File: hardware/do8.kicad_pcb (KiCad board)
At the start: 4 copper layers, 100 x 85 mm, 116 parts, among them J101 TNG-Power-TOP, J102 TNG-Power-BTM, J103 TNG-Data-TOP, J104 TNG-Data-BTM, P102 Debug, P103 PE, P201 OUTPUT0, P202 OUTPUT1, P203 OUTPUT2, P204 OUTPUT3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

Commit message: completely routed
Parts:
- moved Fiducial_Mark 2.00 mm to (101.8, 145.5) (x2)
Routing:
- net VCC: track 31.1 -> 167.2 mm, vias 8 -> 53
- net AGND: track 59.6 -> 163.3 mm, vias 12 -> 95
- net Net-(C202-Pad2): track 34.7 -> 75.1 mm
- net Net-(C211-Pad2): track 36.2 -> 74.1 mm
- net Net-(C203-Pad2): track 25.1 -> 56.6 mm
- net Net-(C209-Pad2): track 25.2 -> 56.1 mm
- net Net-(C121-Pad1): track 19.6 -> 49.9 mm
- net Net-(C120-Pad2): track 13.8 -> 42.1 mm
- net Net-(C204-Pad2): track 21.0 -> 48.1 mm
- net Net-(C119-Pad2): track 11.5 -> 38.1 mm
- net Net-(C207-Pad2): track 20.2 -> 46.3 mm
- net VO: track 33.6 -> 59.0 mm
- net Net-(C206-Pad2): track 12.9 -> 31.9 mm
- net Net-(C205-Pad2): track 12.8 -> 31.4 mm
- net VCCPWRA: track 57.1 -> 62.8 mm
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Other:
- board text removed: "Fläche zur Kühlung mit VCC durchnageln"

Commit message: outline update
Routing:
- net ~CLK: track 57.6 -> 57.0 mm
- net SDO: track 56.0 -> 55.4 mm
- net LED6: track 66.2 -> 65.6 mm
- net ~SS: track 58.8 -> 58.2 mm
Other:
- outline, holes or cut-outs redrawn
- board text added: "DI0"
- board text added: "DI1"
- board text added: "DI2"
- board text added: "DI3"
- board text added: "DI4"
- board text added: "DI5"
- board text added: "DI6"
- board text added: "DI7"
- board text added: "tinkerforge.com"
- board text removed: "DI 0"
- board text removed: "DI 1"
- board text removed: "DI 2"
- board text removed: "DI 3"
- board text removed: "DI 4"
- board text removed: "DI 5"
- board text removed: "DI 6"
- board text removed: "DI 7"

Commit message: fix name
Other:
- board text added: "DO 8P REV 1.0"
- board text removed: "DO8 1.0"
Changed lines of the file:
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@@
     (effects (font (size 1 1) (thickness 0.15)) (justify mirror))
   )
-  (gr_text "DO8 1.0" (at 180.8 144.5) (layer F.SilkS)
+  (gr_text "DO 8P\nREV 1.0" (at 180.8 144.5) (layer F.SilkS)
     (effects (font (size 1 1) (thickness 0.15)))
   )

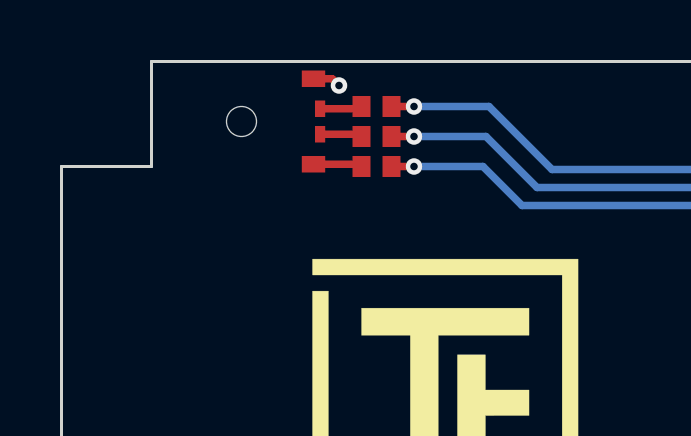
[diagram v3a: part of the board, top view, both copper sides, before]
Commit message: update rgb led drill diameter
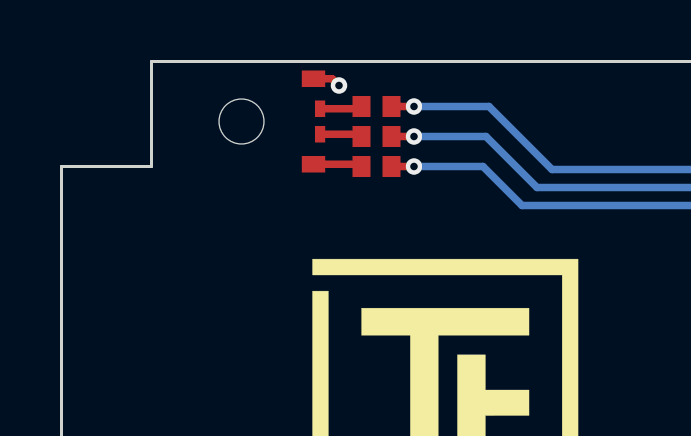
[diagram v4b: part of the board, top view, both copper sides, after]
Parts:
- LED101: footprint LED-RGB-LP -> kicad-libraries:LED-RGB-LP
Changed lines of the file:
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@@
     (add_net USB-DPC)
+  )
+  (module kicad-libraries:LED-RGB-LP (layer F.Cu)
+    (at 98.2 64.5 90)
+    (fp_text reference LED101 (at 0 0 90) (layer F.Fab)
+      (effects (font (size 0.15 0.15) (thickness 0.0375)))
+    )
+    (fp_text value EASV3015RGBA0 (at 0 -0.3 90) (layer F.Fab)
+      (effects (font (size 0.15 0.15) (thickness 0.0375)))
+    )
+    (fp_line (start -1 -1.4) (end 1 -1.4) (layer F.Fab) (width 0.1))
+    (fp_line (start 1 -1.4) (end 1 -8.4) (layer F.Fab) (width 0.1))
+    (fp_line (start 1 -8.4) (end -1 -8.4) (layer F.Fab) (width 0.1))
+    (fp_line (start -1 -8.4) (end -1 -1.4) (layer F.Fab) (width 0.1))
+    (fp_line (start -1.5 -0.5) (end -1.5 0.2) (layer F.Fab) (width 0.025))
+    (fp_line (start 1.5 -0.5) (end -1.5 -0.5) (layer F.Fab) (width 0.025))
+    (fp_line (start 1.5 0.2) (end 1.5 -0.5) (layer F.Fab) (width 0.025))
+    (fp_line (start -1.5 0.2) (end 1.5 0.2) (layer F.Fab) (width 0.025))
+    (fp_arc (start 0 -0.5) (end -0.8 -0.5) (angle 90) (layer F.Fab) (width 0.025))
+    (fp_arc (start 0 -0.5) (end 0 -1.3) (angle 90) (layer F.Fab) (width 0.025))
+    (pad 3 smd rect (at -0.425 0.22 90) (size 0.55 0.34) (layers F.Cu F.Paste F.Mask)
+      (net 33 "Net-(LED101-Pad3)"))
+    (pad 2 smd rect (at 0.425 0.22 90) (size 0.55 0.34) (layers F.Cu F.Paste F.Mask)
+      (net 32 "Net-(LED101-Pad2)"))
+    (pad 4 smd rect (at -1.425 0 90) (size 0.55 0.78) (layers F.Cu F.Paste F.Mask)
+      (net 31 "Net-(LED101-Pad4)"))
+    (pad 1 smd rect (at 1.425 0 90) (size 0.55 0.78) (layers F.Cu F.Paste F.Mask)
+      (net 2 3V3))
+    (pad "" np_thru_hole circle (at 0 -2.4 90) (size 1.5 1.5) (drill 1.5) (layers *.Cu *.Mask))
   )
   (module LED-LP (layer B.Cu)
@@
     )
   )
-  (module LED-RGB-LP (layer F.Cu)
-    (at 98.2 64.5 90)
-    (fp_text reference LED101 (at 0 0 90) (layer F.Fab)
-      (effects (font (size 0.15 0.15) (thickness 0.0375)))
-    )
-    (fp_text value EASV3015RGBA0 (at 0 -0.3 90) (layer F.Fab)
-      (effects (font (size 0.15 0.15) (thickness 0.0375)))
-    )
-    (fp_arc (start 0 -0.5) (end 0 -1.3) (angle 90) (layer F.Fab) (width 0.025))
-    (fp_arc (start 0 -0.5) (end -0.8 -0.5) (angle 90) (layer F.Fab) (width 0.025))
-    (fp_line (start -1.5 0.2) (end 1.5 0.2) (layer F.Fab) (width 0.025))
-    (fp_line (start 1.5 0.2) (end 1.5 -0.5) (layer F.Fab) (width 0.025))
-    (fp_line (start 1.5 -0.5) (end -1.5 -0.5) (layer F.Fab) (width 0.025))
-    (fp_line (start -1.5 -0.5) (end -1.5 0.2) (layer F.Fab) (width 0.025))
-    (fp_line (start -1 -8.4) (end -1 -1.4) (layer F.Fab) (width 0.1))
-    (fp_line (start 1 -8.4) (end -1 -8.4) (layer F.Fab) (width 0.1))
-    (fp_line (start 1 -1.4) (end 1 -8.4) (layer F.Fab) (width 0.1))
-    (fp_line (start -1 -1.4) (end 1 -1.4) (layer F.Fab) (width 0.1))
-    (pad "" np_thru_hole circle (at 0 -2.4 90) (size 1 1) (drill 1) (layers *.Cu *.Mask))
-    (pad 1 smd rect (at 1.425 0 90) (size 0.55 0.78) (layers F.Cu F.Paste F.Mask)
-      (net 2 3V3))
-    (pad 4 smd rect (at -1.425 0 90) (size 0.55 0.78) (layers F.Cu F.Paste F.Mask)
-      (net 31 "Net-(LED101-Pad4)"))
-    (pad 2 smd rect (at 0.425 0.22 90) (size 0.55 0.34) (layers F.Cu F.Paste F.Mask)
-      (net 32 "Net-(LED101-Pad2)"))
-    (pad 3 smd rect (at -0.425 0.22 90) (size 0.55 0.34) (layers F.Cu F.Paste F.Mask)
-      (net 33 "Net-(LED101-Pad3)"))
-  )
   (module kicad-libraries:Logo_TF_10x12 (layer F.Cu)

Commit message: fix inductor footprint
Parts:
- LED101: footprint kicad-libraries:LED-RGB-LP -> LED-RGB-LP
- turned T101 to 180 degrees
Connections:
- T101 pad 1: Net-(C120-Pad2) -> Net-(C121-Pad1)
- T101 pad 3: Net-(C121-Pad1) -> Net-(C120-Pad2)
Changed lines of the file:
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@@
     (add_net USB-DPC)
   )
-  (module kicad-libraries:LED-RGB-LP (layer F.Cu)
-    (at 98.2 64.5 90)
-    (fp_text reference LED101 (at 0 0 90) (layer F.Fab)
+  (module kicad-libraries:WE-SL5 (layer F.Cu)
+    (at 150.5 135.65 180)
+    (fp_text reference T101 (at 0 0.5) (layer F.Fab)
       (effects (font (size 0.15 0.15) (thickness 0.0375)))
     )
-    (fp_text value EASV3015RGBA0 (at 0 -0.3 90) (layer F.Fab)
+    (fp_text value 744273222 (at 0 -0.5) (layer F.Fab)
       (effects (font (size 0.15 0.15) (thickness 0.0375)))
     )
-    (fp_line (start -1 -1.4) (end 1 -1.4) (layer F.Fab) (width 0.1))
-    (fp_line (start 1 -1.4) (end 1 -8.4) (layer F.Fab) (width 0.1))
-    (fp_line (start 1 -8.4) (end -1 -8.4) (layer F.Fab) (width 0.1))
-    (fp_line (start -1 -8.4) (end -1 -1.4) (layer F.Fab) (width 0.1))
-    (fp_line (start -1.5 -0.5) (end -1.5 0.2) (layer F.Fab) (width 0.025))
-    (fp_line (start 1.5 -0.5) (end -1.5 -0.5) (layer F.Fab) (width 0.025))
-    (fp_line (start 1.5 0.2) (end 1.5 -0.5) (layer F.Fab) (width 0.025))
-    (fp_line (start -1.5 0.2) (end 1.5 0.2) (layer F.Fab) (width 0.025))
-    (fp_arc (start 0 -0.5) (end -0.8 -0.5) (angle 90) (layer F.Fab) (width 0.025))
-    (fp_arc (start 0 -0.5) (end 0 -1.3) (angle 90) (layer F.Fab) (width 0.025))
-    (pad 3 smd rect (at -0.425 0.22 90) (size 0.55 0.34) (layers F.Cu F.Paste F.Mask)
-      (net 33 "Net-(LED101-Pad3)"))
-    (pad 2 smd rect (at 0.425 0.22 90) (size 0.55 0.34) (layers F.Cu F.Paste F.Mask)
-      (net 32 "Net-(LED101-Pad2)"))
-    (pad 4 smd rect (at -1.425 0 90) (size 0.55 0.78) (layers F.Cu F.Paste F.Mask)
-      (net 31 "Net-(LED101-Pad4)"))
-    (pad 1 smd rect (at 1.425 0 90) (size 0.55 0.78) (layers F.Cu F.Paste F.Mask)
-      (net 2 3V3))
-    (pad "" np_thru_hole circle (at 0 -2.4 90) (size 1.5 1.5) (drill 1.5) (layers *.Cu *.Mask))
+    (fp_line (start -5 4.4) (end -5 -4.4) (layer F.Fab) (width 0.1))
+    (fp_line (start 5 4.4) (end -5 4.4) (layer F.Fab) (width 0.1))
+    (fp_line (start 5 -4.4) (end 5 4.4) (layer F.Fab) (width 0.1))
+    (fp_line (start -5 -4.4) (end 5 -4.4) (layer F.Fab) (width 0.1))
+    (fp_circle (center -3.5 -2) (end -3.2 -1.7) (layer F.Fab) (width 0.1))
+    (pad 2 smd rect (at -3.81 3.11 180) (size 2.7 2.7) (layers F.Cu F.Paste F.Mask)
+      (net 53 AGNDA))
+    (pad 3 smd rect (at 3.81 3.11 180) (size 2.7 2.7) (layers F.Cu F.Paste F.Mask)
+      (net 64 "Net-(C120-Pad2)"))
+    (pad 4 smd rect (at 3.81 -3.11 180) (size 2.7 2.7) (layers F.Cu F.Paste F.Mask)
+      (net 45 "Net-(C119-Pad2)"))
+    (pad 1 smd rect (at -3.81 -3.11 180) (size 2.7 2.7) (layers F.Cu F.Paste F.Mask)
+      (net 56 "Net-(C121-Pad1)"))
+    (model ${KICAD_SYMBOL_DIR}/3d/Inductors/WE-SL5.wrl
+      (at (xyz 0 0 0))
+      (scale (xyz 1 1 1))
+      (rotate (xyz 0 0 0))
+    )
   )
   (module LED-LP (layer B.Cu)
@@
     )
   )
-  (module kicad-libraries:WE-SL5 (layer F.Cu)
-    (at 150.5 135.65)
-    (fp_text reference T101 (at 0 0.5) (layer F.Fab)
-      (effects (font (size 0.15 0.15) (thickness 0.0375)))
-    )
-    (fp_text value 744273222 (at 0 -0.5) (layer F.Fab)
-      (effects (font (size 0.15 0.15) (thickness 0.0375)))
-    )
-    (fp_line (start -5 4.4) (end -5 -4.4) (layer F.Fab) (width 0.1))
-    (fp_line (start 5 4.4) (end -5 4.4) (layer F.Fab) (width 0.1))
-    (fp_line (start 5 -4.4) (end 5 4.4) (layer F.Fab) (width 0.1))
-    (fp_line (start -5 -4.4) (end 5 -4.4) (layer F.Fab) (width 0.1))
-    (fp_circle (center -3.5 1.5) (end -3.2 1.8) (layer F.Fab) (width 0.1))
-    (pad 4 smd rect (at -3.81 3.11) (size 2.7 2.7) (layers F.Cu F.Paste F.Mask)
-      (net 45 "Net-(C119-Pad2)"))
-    (pad 3 smd rect (at 3.81 3.11) (size 2.7 2.7) (layers F.Cu F.Paste F.Mask)
-      (net 56 "Net-(C121-Pad1)"))
-    (pad 2 smd rect (at 3.81 -3.11) (size 2.7 2.7) (layers F.Cu F.Paste F.Mask)
-      (net 53 AGNDA))
-    (pad 1 smd rect (at -3.81 -3.11) (size 2.7 2.7) (layers F.Cu F.Paste F.Mask)
-      (net 64 "Net-(C120-Pad2)"))
-    (model Inductors/WE-SL5.wrl
-      (at (xyz 0 0 0))
-      (scale (xyz 1 1 1))
-      (rotate (xyz 0 0 0))
-    )
-  )
   (module C0402F (layer F.Cu)
     (at 156.85 98 90)
@@
       (net 13 AGND))
   )
+  (module LED-RGB-LP (layer F.Cu)
+    (at 98.2 64.5 90)
+    (fp_text reference LED101 (at 0 0 90) (layer F.Fab)
+      (effects (font (size 0.15 0.15) (thickness 0.0375)))
+    )
+    (fp_text value EASV3015RGBA0 (at 0 -0.3 90) (layer F.Fab)
+      (effects (font (size 0.15 0.15) (thickness 0.0375)))
+    )
+    (fp_arc (start 0 -0.5) (end 0 -1.3) (angle 90) (layer F.Fab) (width 0.025))
+    (fp_arc (start 0 -0.5) (end -0.8 -0.5) (angle 90) (layer F.Fab) (width 0.025))
+    (fp_line (start -1.5 0.2) (end 1.5 0.2) (layer F.Fab) (width 0.025))
+    (fp_line (start 1.5 0.2) (end 1.5 -0.5) (layer F.Fab) (width 0.025))
+    (fp_line (start 1.5 -0.5) (end -1.5 -0.5) (layer F.Fab) (width 0.025))
+    (fp_line (start -1.5 -0.5) (end -1.5 0.2) (layer F.Fab) (width 0.025))
+    (fp_line (start -1 -8.4) (end -1 -1.4) (layer F.Fab) (width 0.1))
+    (fp_line (start 1 -8.4) (end -1 -8.4) (layer F.Fab) (width 0.1))
+    (fp_line (start 1 -1.4) (end 1 -8.4) (layer F.Fab) (width 0.1))
+    (fp_line (start -1 -1.4) (end 1 -1.4) (layer F.Fab) (width 0.1))
+    (pad "" np_thru_hole circle (at 0 -2.4 90) (size 1.5 1.5) (drill 1.5) (layers *.Cu *.Mask))
+    (pad 1 smd rect (at 1.425 0 90) (size 0.55 0.78) (layers F.Cu F.Paste F.Mask)
+      (net 2 3V3))
+    (pad 4 smd rect (at -1.425 0 90) (size 0.55 0.78) (layers F.Cu F.Paste F.Mask)
+      (net 31 "Net-(LED101-Pad4)"))
+    (pad 2 smd rect (at 0.425 0.22 90) (size 0.55 0.34) (layers F.Cu F.Paste F.Mask)
+      (net 32 "Net-(LED101-Pad2)"))
+    (pad 3 smd rect (at -0.425 0.22 90) (size 0.55 0.34) (layers F.Cu F.Paste F.Mask)
+      (net 33 "Net-(LED101-Pad3)"))
+  )
   (gr_text tinkerforge.com (at 180.8 144.5) (layer B.SilkS)

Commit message: fix description
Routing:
- net VCCPWRA: track 62.8 -> 60.7 mm, vias 13 -> 12
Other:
- board text added: "DO0"
- board text added: "DO1"
- board text added: "DO2"
- board text added: "DO3"
- board text added: "DO4"
- board text added: "DO5"
- board text added: "DO6"
- board text added: "DO7"
- board text removed: "DI0"
- board text removed: "DI1"
- board text removed: "DI2"
- board text removed: "DI3"
- board text removed: "DI4"
- board text removed: "DI5"
- board text removed: "DI6"
- board text removed: "DI7"
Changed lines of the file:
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@@
     (thickness 1.6)
     (drawings 30)
-    (tracks 1833)
+    (tracks 1830)
     (zones 0)
     (modules 116)
@@
   (layers
     (0 F.Cu signal)
-    (1 GND power)
-    (2 VCC power)
+    (1 GND power hide)
+    (2 VCC power hide)
     (31 B.Cu signal)
     (32 B.Adhes user)
@@
     (mod_text_size 1 1)
     (mod_text_width 0.15)
-    (pad_size 1.5 1.5)
-    (pad_drill 0.6)
+    (pad_size 1.6 2.15)
+    (pad_drill 0)
     (pad_to_mask_clearance 0)
     (solder_mask_min_width 0.25)
@@
     (pad 2 smd rect (at 2.11 0) (size 1.62 2.18) (layers F.Cu F.Paste F.Mask)
       (net 13 AGND))
-    (pad 1 smd rect (at -2.11 0) (size 1.62 2.18) (layers F.Cu F.Paste F.Mask)
+    (pad 1 smd rect (at -2.11 0) (size 1.6 2.15) (layers F.Cu F.Paste F.Mask)
       (net 68 "Net-(C211-Pad2)"))
   )
@@
     (pad 2 smd rect (at 2.11 0) (size 1.62 2.18) (layers F.Cu F.Paste F.Mask)
       (net 13 AGND))
-    (pad 1 smd rect (at -2.11 0) (size 1.62 2.18) (layers F.Cu F.Paste F.Mask)
+    (pad 1 smd rect (at -2.11 0) (size 1.6 2.15) (layers F.Cu F.Paste F.Mask)
       (net 18 "Net-(C207-Pad2)"))
   )
@@
     (pad 2 smd rect (at 2.11 0) (size 1.62 2.18) (layers F.Cu F.Paste F.Mask)
       (net 13 AGND))
-    (pad 1 smd rect (at -2.11 0) (size 1.62 2.18) (layers F.Cu F.Paste F.Mask)
+    (pad 1 smd rect (at -2.11 0) (size 1.6 2.15) (layers F.Cu F.Paste F.Mask)
       (net 16 "Net-(C205-Pad2)"))
   )
@@
     (pad 2 smd rect (at 2.11 0) (size 1.62 2.18) (layers F.Cu F.Paste F.Mask)
       (net 13 AGND))
-    (pad 1 smd rect (at -2.11 0) (size 1.62 2.18) (layers F.Cu F.Paste F.Mask)
+    (pad 1 smd rect (at -2.11 0) (size 1.6 2.15) (layers F.Cu F.Paste F.Mask)
       (net 15 "Net-(C203-Pad2)"))
   )
@@
     (fp_line (start 2.3 2) (end -2.3 2) (layer F.SilkS) (width 0.15))
     (fp_line (start -2.3 2) (end -2.3 -2) (layer F.SilkS) (width 0.15))
-    (pad 1 smd rect (at -2.11 0) (size 1.62 2.18) (layers F.Cu F.Paste F.Mask)
+    (pad 1 smd rect (at -2.11 0) (size 1.6 2.15) (layers F.Cu F.Paste F.Mask)
       (net 19 "Net-(C209-Pad2)"))
     (pad 2 smd rect (at 2.11 0) (size 1.62 2.18) (layers F.Cu F.Paste F.Mask)
@@
     (fp_line (start 2.3 2) (end -2.3 2) (layer F.SilkS) (width 0.15))
     (fp_line (start -2.3 2) (end -2.3 -2) (layer F.SilkS) (width 0.15))
-    (pad 1 smd rect (at -2.11 0) (size 1.62 2.18) (layers F.Cu F.Paste F.Mask)
+    (pad 1 smd rect (at -2.11 0) (size 1.6 2.15) (layers F.Cu F.Paste F.Mask)
       (net 17 "Net-(C206-Pad2)"))
     (pad 2 smd rect (at 2.11 0) (size 1.62 2.18) (layers F.Cu F.Paste F.Mask)
@@
     (fp_line (start 2.3 2) (end -2.3 2) (layer F.SilkS) (width 0.15))
     (fp_line (start -2.3 2) (end -2.3 -2) (layer F.SilkS) (width 0.15))
-    (pad 1 smd rect (at -2.11 0) (size 1.62 2.18) (layers F.Cu F.Paste F.Mask)
+    (pad 1 smd rect (at -2.11 0) (size 1.6 2.15) (layers F.Cu F.Paste F.Mask)
       (net 67 "Net-(C204-Pad2)"))
     (pad 2 smd rect (at 2.11 0) (size 1.62 2.18) (layers F.Cu F.Paste F.Mask)
@@
     (fp_line (start 2.3 2) (end -2.3 2) (layer F.SilkS) (width 0.15))
     (fp_line (start -2.3 2) (end -2.3 -2) (layer F.SilkS) (width 0.15))
-    (pad 1 smd rect (at -2.11 0) (size 1.62 2.18) (layers F.Cu F.Paste F.Mask)
+    (pad 1 smd rect (at -2.11 0) (size 1.6 2.15) (layers F.Cu F.Paste F.Mask)
       (net 14 "Net-(C202-Pad2)"))
     (pad 2 smd rect (at 2.11 0) (size 1.62 2.18) (layers F.Cu F.Paste F.Mask)
@@
     (effects (font (size 1 1) (thickness 0.15)) (justify mirror))
   )
-  (gr_text DI7 (at 93.8 139.3 90) (layer B.SilkS)
+  (gr_text DO7 (at 93.8 139.3 90) (layer B.SilkS)
     (effects (font (size 1 1) (thickness 0.15)) (justify mirror))
   )
-  (gr_text DI6 (at 93.8 135.9 90) (layer B.SilkS)
+  (gr_text DO6 (at 93.8 135.9 90) (layer B.SilkS)
     (effects (font (size 1 1) (thickness 0.15)) (justify mirror))
   )
@@
     (effects (font (size 1 1) (thickness 0.15)) (justify mirror))
   )
-  (gr_text DI5 (at 93.8 123.3 90) (layer B.SilkS)
+  (gr_text DO5 (at 93.8 123.3 90) (layer B.SilkS)
     (effects (font (size 1 1) (thickness 0.15)) (justify mirror))
   )
-  (gr_text DI4 (at 93.8 119.8 90) (layer B.SilkS)
+  (gr_text DO4 (at 93.8 119.8 90) (layer B.SilkS)
     (effects (font (size 1 1) (thickness 0.15)) (justify mirror))
   )
@@
     (effects (font (size 1 1) (thickness 0.15)) (justify mirror))
   )
-  (gr_text DI3 (at 93.8 107.3 90) (layer B.SilkS)
+  (gr_text DO3 (at 93.8 107.3 90) (layer B.SilkS)
     (effects (font (size 1 1) (thickness 0.15)) (justify mirror))
   )
-  (gr_text DI2 (at 93.8 103.8 90) (layer B.SilkS)
+  (gr_text DO2 (at 93.8 103.8 90) (layer B.SilkS)
     (effects (font (size 1 1) (thickness 0.15)) (justify mirror))
   )
@@
     (effects (font (size 1 1) (thickness 0.15)) (justify mirror))
   )
-  (gr_text DI1 (at 93.8 91.3 90) (layer B.SilkS)
+  (gr_text DO1 (at 93.8 91.3 90) (layer B.SilkS)
     (effects (font (size 1 1) (thickness 0.15)) (justify mirror))
   )
@@
     (effects (font (size 1 1) (thickness 0.15)) (justify mirror))
   )
-  (gr_text DI0 (at 93.8 87.9 90) (layer B.SilkS)
+  (gr_text DO0 (at 93.8 87.9 90) (layer B.SilkS)
     (effects (font (size 1 1) (thickness 0.15)) (justify mirror))
   )
@@
   (segment (start 170.15 124.1) (end 170.15 124.55) (width 0.4) (layer B.Cu) (net 54))
   (segment (start 170.15 124.55) (end 169.65 125.05) (width 0.4) (layer B.Cu) (net 54))
-  (via (at 172 124.1) (size 0.55) (drill 0.25) (layers F.Cu B.Cu) (net 54))
-  (segment (start 172.75 124.1) (end 172 124.1) (width 0.3) (layer B.Cu) (net 54))
-  (segment (start 172 124.1) (end 170.6 124.1) (width 0.3) (layer F.Cu) (net 54))
   (segment (start 170.6 124.1) (end 169.65 125.05) (width 0.3) (layer F.Cu) (net 54))
   (via (at 170.85 120.5) (size 0.55) (drill 0.25) (layers F.Cu B.Cu) (net 54))
